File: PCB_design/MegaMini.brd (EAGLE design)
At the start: 62.2 x 44.1 mm, 24 parts, among them IC1 2560-16AU, IC2 DS1307, J1 AVR_SPI_PROG_3X2NS

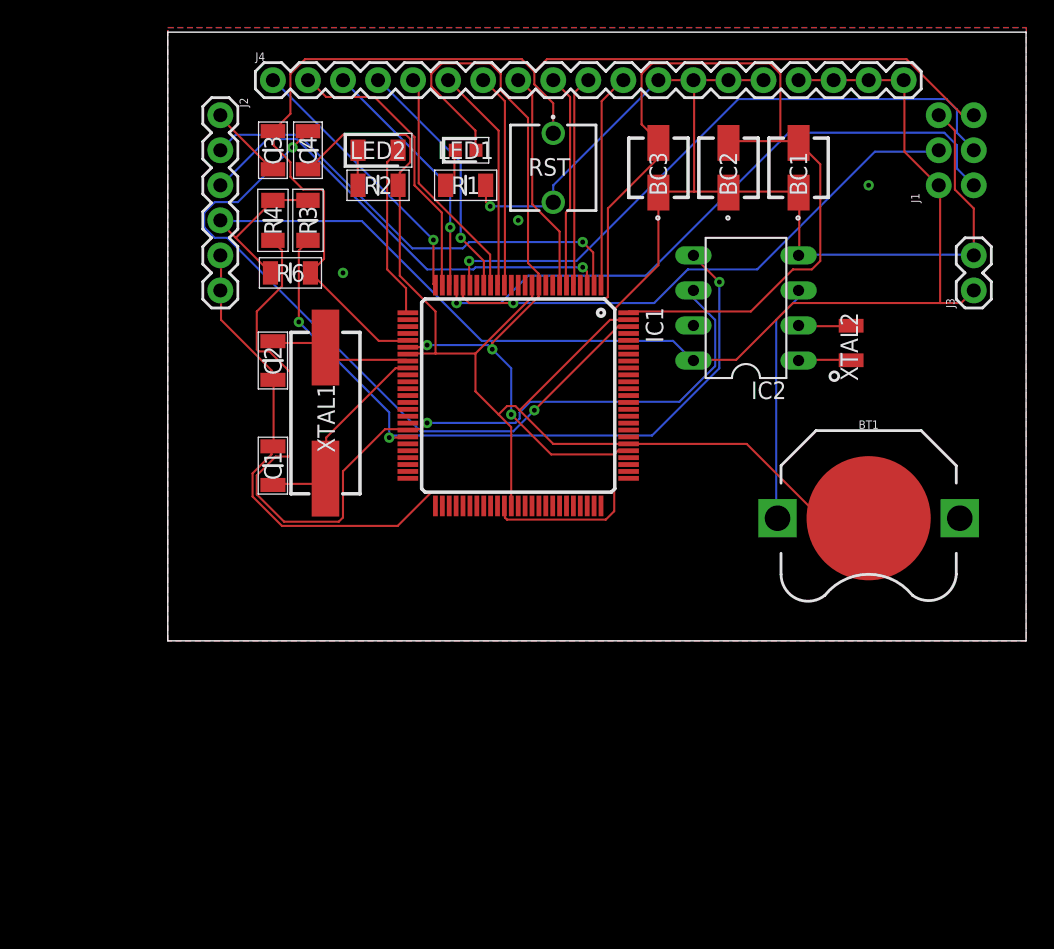
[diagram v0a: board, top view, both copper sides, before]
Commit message: Finished revision 1.0 PCB and some major changes to the schematic
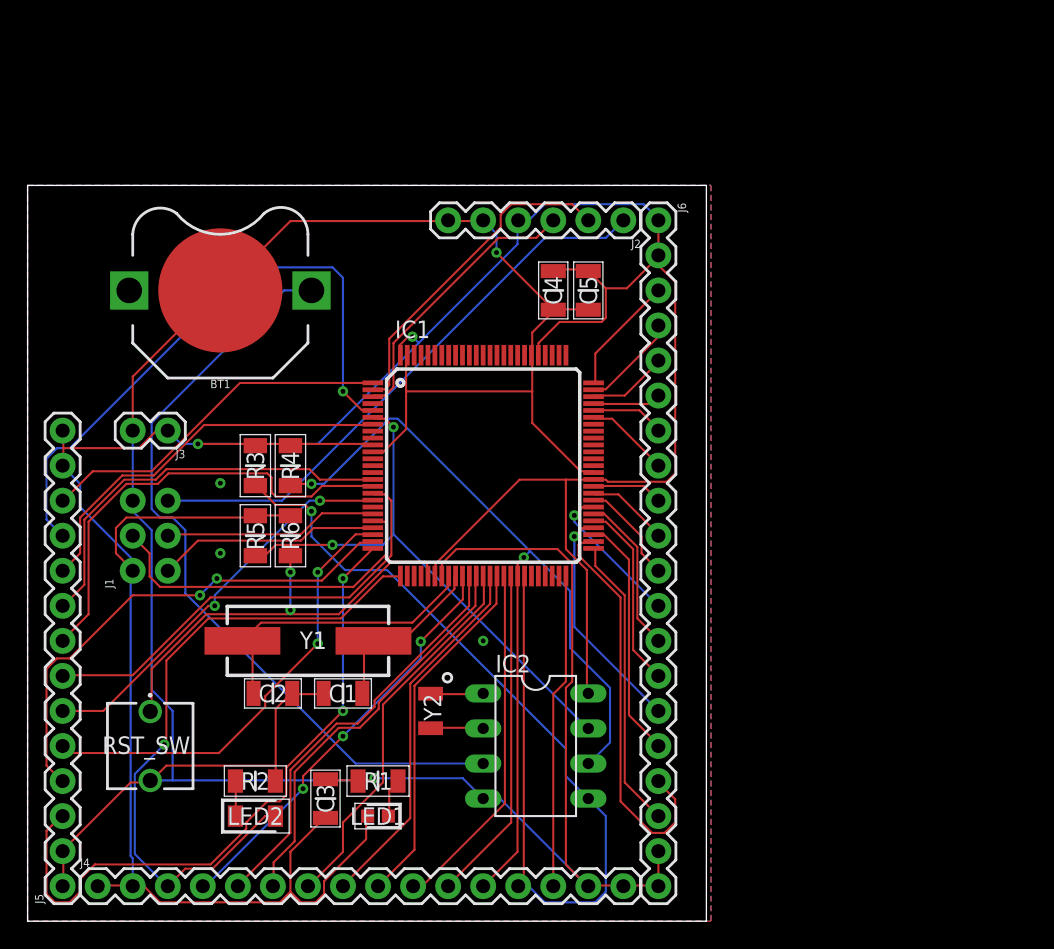
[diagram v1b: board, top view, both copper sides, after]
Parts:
- removed BC1, BC2, BC3: 0.1µF, C_WCAP-AS5H Series:865230640001
- removed RST: FSM4JRT, C_FSM4JRT:FSM4JRT
- removed XTAL1: 16MHz, CL=10pF, C_FOXSDLF_160-20:FOXSDLF/120-20
- removed XTAL2: 32.768KHz, C_Q13FC13500004_FC-135_32.768KHZ:FC-135
- added C5: 0.1µF, C_C1206C104K5RACTU:CAPC3216X88N
- added J5: (no value), SparkFun-Connectors:1X14
- added J6: (no value), SparkFun-Connectors:1X20
- added R5: 10K, C_ERJ8ENF1002V:RESC3116X70N
- added RST_SW: FSM4JRT, C_FSM4JRT:FSM4JRT
- added Y1: 16MHz, C_FOXSDLF_160-20:FOXSDLF/120-20
- added Y2: 32.768KHz, C_Q13FC13500004_FC-135_32.768KHZ:FC-135
- BT1: value Keystone 3001 -> (none)
- C3, C4: device C_MC1206B104K500CT:CAPC3216X90N -> C_C1206C104K5RACTU:CAPC3216X88N
- J4: device SparkFun-Connectors:1X19 -> SparkFun-Connectors:1X16
- R1, R2: value 10K -> 470; device C_ERJ8ENF1002V:RESC3116X70N -> C_ERJ8ENF4700V:RESC3116X70N
- moved J1 64.8 mm to (8.89, 27.9)
- moved J4 59.8 mm to (5.08, 2.54)
- moved J3 59.3 mm to (10.2, 35.6), turned to 180 degrees
- moved BT1 49.8 mm to (14.0, 45.7), turned to 0 degrees
- moved LED2 49.1 mm to (16.5, 7.62)
- moved LED1 48.7 mm to (25.4, 7.62), turned to 180 degrees
- moved C3 47.1 mm to (21.6, 8.89), turned to 270 degrees
- moved R2 44.1 mm to (16.5, 10.2), turned to 0 degrees
- moved R1 43.6 mm to (25.4, 10.2), turned to 0 degrees
- moved IC2 35.2 mm to (36.8, 12.7), turned to 270 degrees
- moved J2 30.2 mm to (43.2, 50.8), turned to 180 degrees
- moved C2 24.1 mm to (17.8, 16.5), turned to 0 degrees
- moved C4 20.5 mm to (38.1, 45.7)
- moved R6 19.1 mm to (19.1, 27.9), turned to 90 degrees
- moved R3 18.2 mm to (16.5, 33.0)
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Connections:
- removed net 5V: BC1.2, BC2.2, BC3.2, IC1.10, IC1.100, IC1.31, IC1.61, IC1.80, LED1.2
- removed net AREF: C4.2, IC1.98
- removed net DTR: C3.1, J2.1
- removed net N$2: LED2.1, R2.2
- removed net SQW/OUT: IC2.7
- new net N$1: IC1.30, R6.1, RST_SW.1
- new net N$15: LED2.1, R2.1
- new net PA3: IC1.75, J6.3
- new net PA4: IC1.74, J6.4
- new net PA5: IC1.73, J6.5
- new net PA6: IC1.72, J6.6
- new net PA7: IC1.71, J6.7
- new net PC0: IC1.53, J6.16
- new net PC1: IC1.54, J6.15
- new net PC2: IC1.55, J6.14
- new net PC3: IC1.56, J6.13
- new net PC4: IC1.57, J6.12
- new net PC5: IC1.58, J6.11
- new net PC6: IC1.59, J6.10
- new net PC7: IC1.60, J6.9
- new net PD7: IC1.50, J4.14
- new net PG0: IC1.51, J6.18
- new net PG1: IC1.52, J6.17
- new net PG2: IC1.70, J6.8
- new net PL0: IC1.35, J4.4
- new net PL1: IC1.36, J4.5
- new net PL2: IC1.37, J4.6
- new net PL3: IC1.38, J4.7
- new net PL4: IC1.39, J4.8
- new net PL5: IC1.40, J4.9
- new net PL6: IC1.41, J4.10
- new net PL7: IC1.42, J4.11
- net GND: now also C2.2, C3.1, C5.1, J4.16, J5.1, J5.2, J6.19, J6.20, R2.2, RST_SW.2; no longer BC1.1, BC2.1, BC3.1, C2.1, J4.12, J4.13, J4.14, R2.1, RST.2
- net N$3: now also Y2.1; no longer XTAL2.1
- net N$4: now also Y2.2; no longer XTAL2.2
- net PB4: now also J5.5; no longer J4.3
- net PB5: now also J5.4; no longer J4.2
- net PB6: now also J5.3; no longer J4.1
- net PB7: now also J4.3
- net PD0: now also J4.12
- net PD1: now also J4.13
- net PE3: now also J5.11; no longer J4.10
- net PE4: now also IC2.7, R5.2; no longer J4.9
- net PE5: now also J5.10; no longer J4.8
- net PG5: now also J5.12; no longer J4.11
- net PH3: now also J5.9; no longer J4.7
- net PH4: now also J5.8; no longer J4.6
- net PH5: now also J5.7; no longer J4.5
- net PH6: now also J5.6; no longer J4.4
- net RST: now also J2.1; no longer C3.2, IC1.30, R6.1, RST.1
- net VCC: now also C3.2, C4.2, C5.2, IC1.10, IC1.100, IC1.31, IC1.61, IC1.80, J4.1, J4.2, J5.13, J5.14, J6.1, J6.2, LED1.2, R5.1; no longer J4.16, J4.17, J4.18, J4.19
- net XTAL1: now also Y1.1; no longer XTAL1.1
- net XTAL2: now also C2.1, Y1.2; no longer C2.2, XTAL1.2
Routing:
- net 5V: track 138.6 -> 0.00 mm, vias 3 -> 0
- net VCC: track 97.7 -> 226.0 mm, vias 0 -> 2
- net AREF: track 51.1 -> 0.00 mm, vias 2 -> 0
- net RST: track 84.3 -> 41.4 mm
- net N$24: track 17.3 -> 56.2 mm
- net PB7: track 12.7 -> 47.7 mm, vias 0 -> 1
- net N$1: track 0.00 -> 31.5 mm, vias 0 -> 2
- net PL0: track 0.00 -> 30.5 mm, vias 0 -> 3
- net PL1: track 0.00 -> 30.3 mm
- net MISO: track 46.5 -> 16.2 mm, vias 1 -> 0
- net SCK: track 45.8 -> 15.6 mm, vias 1 -> 0
- net PG1: track 0.00 -> 29.8 mm
- net PL2: track 0.00 -> 29.5 mm
- net PE3: track 15.4 -> 44.6 mm, vias 0 -> 1
- net PB6: track 19.8 -> 48.3 mm, vias 1 -> 2
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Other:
- board size 62.2 x 44.1 mm -> 49.2 x 53.3 mm
